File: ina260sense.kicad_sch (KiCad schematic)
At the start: 2 parts, among them U23 INA260

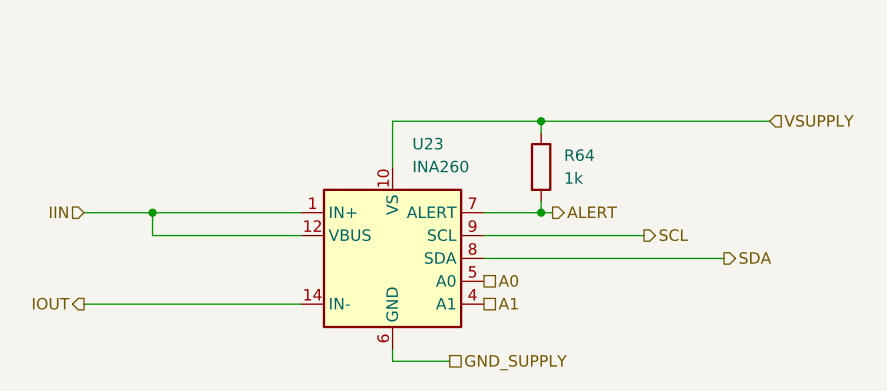
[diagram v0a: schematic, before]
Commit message: added footprints to almost all components
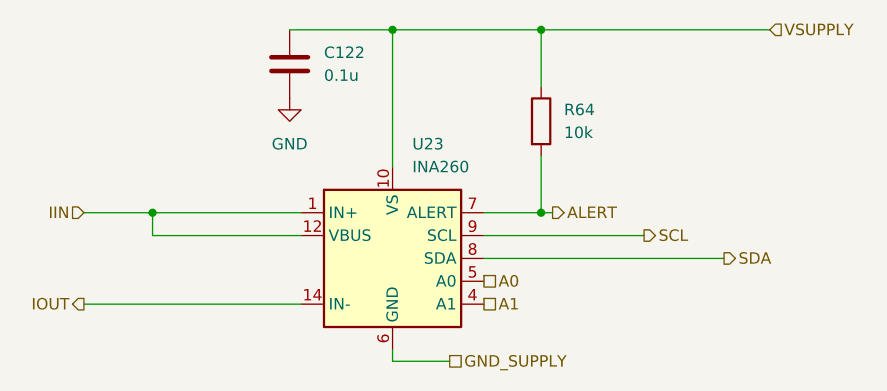
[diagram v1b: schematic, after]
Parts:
- added C122: 0.1u, Capacitor_SMD:C_0603_1608Metric_Pad1.08x0.95mm_HandSolder, symbol Device:C
- R64: value 1k -> 10k; footprint (none) -> Resistor_SMD:R_0805_2012Metric_Pad1.20x1.40mm_HandSolder
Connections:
- net VSUPPLY: now also C122.1
- new net GND: C122.2
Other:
- moved on the sheet: R64
